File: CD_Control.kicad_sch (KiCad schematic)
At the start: 61 parts, among them Q10 ASR65R046EFD, Q11 ASR65R046EFD, Q12 ASR65R046EFD, Q13 ASR65R046EFD, Q14 ASR65R046EFD, Q15 ASR65R046EFD, Q16 ASR65R046EFD, Q17 AO3400A, Q18 AO3400A, Q19 ASR65R046EFD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

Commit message: More sims, more buildout
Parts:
- added R35: 0.3mR, symbol ct_lib:SEWF3951DL300P9
- added R36: 0Ω, PCM_JLCPCB:R_0402, symbol PCM_JLCPCB-Resistors:0402,0Ω
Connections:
- net GND: now also R36.1
- net PACK_NEGATIVE renamed GNDPWR
- net GNDPWR: now also R35.1
- new net CELLS_NEGATIVE: R35.2, R36.2
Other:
- note added: "Current gain, helps turn-on time Optional"
- note added: "Fast turn-off Optional"
- note added: "Measure range: +/-667 A Trip range: +/-1,667 A"
- note added: "TODO"
- note removed: "Current gain, helps turn-on time"
- note removed: "Fast turn-off"

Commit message: isolated comms
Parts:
- JP1, JP2: footprint Jumper:SolderJumper-2_P1.3mm_Open_TrianglePad1.0x1.5mm -> Jumper:SolderJumper-2_P1.3mm_Open_RoundedPad1.0x1.5mm
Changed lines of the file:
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@@
 			)
 		)
-		(property "Footprint" "Jumper:SolderJumper-2_P1.3mm_Open_TrianglePad1.0x1.5mm"
+		(property "Footprint" "Jumper:SolderJumper-2_P1.3mm_Open_RoundedPad1.0x1.5mm"
 			(at 125.73 213.36 0)
 			(effects
@@
 			)
 		)
-		(property "Footprint" "Jumper:SolderJumper-2_P1.3mm_Open_TrianglePad1.0x1.5mm"
+		(property "Footprint" "Jumper:SolderJumper-2_P1.3mm_Open_RoundedPad1.0x1.5mm"
 			(at 210.82 193.04 0)
 			(effects

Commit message: rolled back TO commit caa5444, didn't mean to roll THAT back
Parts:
- removed D14, D16: D, symbol Device:D
- added D16: MMSZ5246B, PCM_JLCPCB:D_SOD-123, symbol PCM_JLCPCB-Diodes:Zener,MMSZ5246B
- added D22: SMCJ100A_C42371542, JLCImport:SMCJ100A_C42371542, symbol JLCImport:SMCJ100A_C42371542
- added Q22: FQD3P50TM, PCM_JLCPCB:TO-252-2_L6.5-W6.1-P4.58-LS10.0-TL, symbol JLCImport:FQD3P50TM
- added R71, R72, R73: 620R, PCM_JLCPCB:R_1206, symbol ct_lib:1206W4F6200T5E
- added R76: 47kΩ, PCM_JLCPCB:R_0402, symbol PCM_JLCPCB-Resistors:0402,47kΩ
- added R77: 10MΩ, PCM_JLCPCB:R_0402, symbol PCM_JLCPCB-Resistors:0402,10MΩ
- added U10: SMCJ440A_C5294117, PCM_JLCPCB:SOIC-8_L4.9-W3.9-P1.27-LS6.0-BL, symbol JLCImport:SMCJ440A_C5294117
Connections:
- net GNDPWR: now also U10.1 (C)
- net PACK_POSITIVE: now also C11.2, D22.1 (C), R71.2
- net PDSG_GATE_CTRL: now also R76.2
- net at Q10.3 (D), Q11.3 (D), Q12.3 (D)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: now also D16.2, Q22.3 (S), R77.1
- new net: R72.1, R73.1
- new net: R72.2, R73.2
- new net: D22.2 (A), U10.2 (A)
- new net: D16.1, Q22.1 (G), R76.1, R77.2
- new net: Q22.2 (D), R71.1
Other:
- note added: "100V to -440V"
- note added: "500V_SD"
- note added: "650V_DS"
- note added: "Charge"
- note added: "Clamp gate w/ negative terminal voltage"
- note added: "Discharge"
- note added: "Precharge"
- note removed: "120? up 440 down"
- note removed: "450V_DS"
- note removed: "Clamp gate w/ negative terminal voltage Limit: -450V"
- note removed: "Precharge circuit?"
- note removed: "SMBJ440A"
- note removed: "TODO"
- moved on the sheet: C11, C9, D10, D11, D12, D13, D15, D7, D8, D9, JP1, JP2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

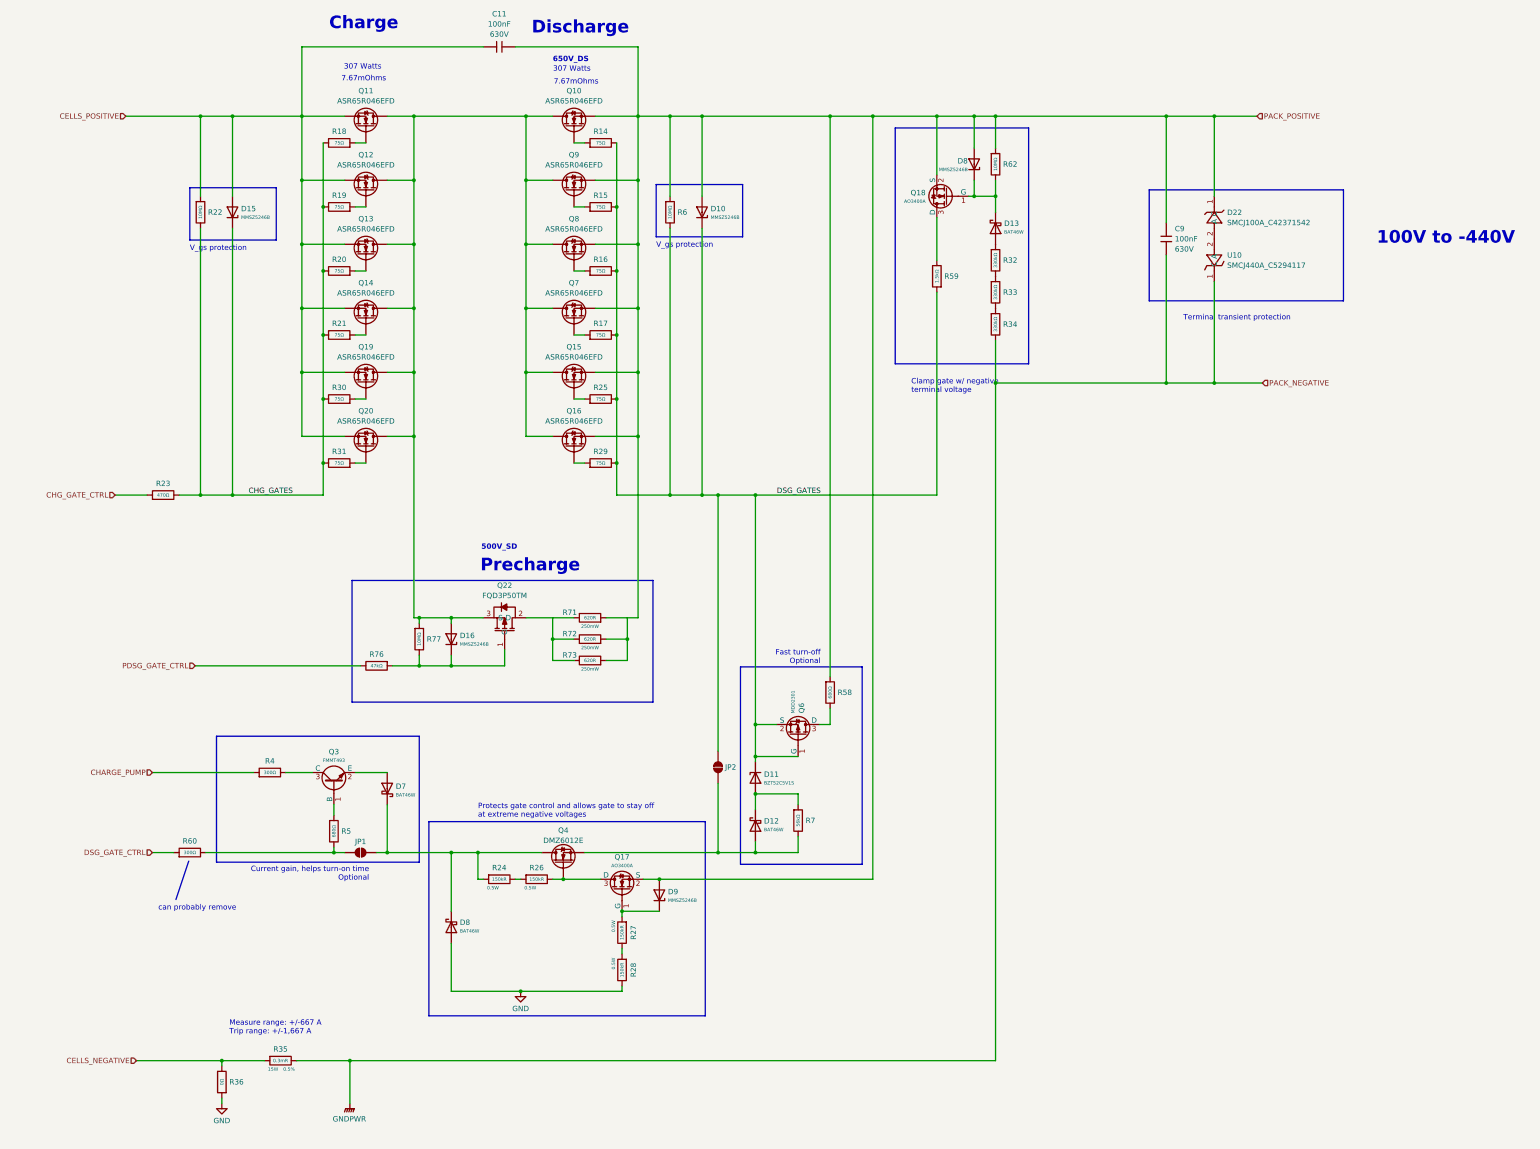
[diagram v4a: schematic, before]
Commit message: prepping for split into 2 boards
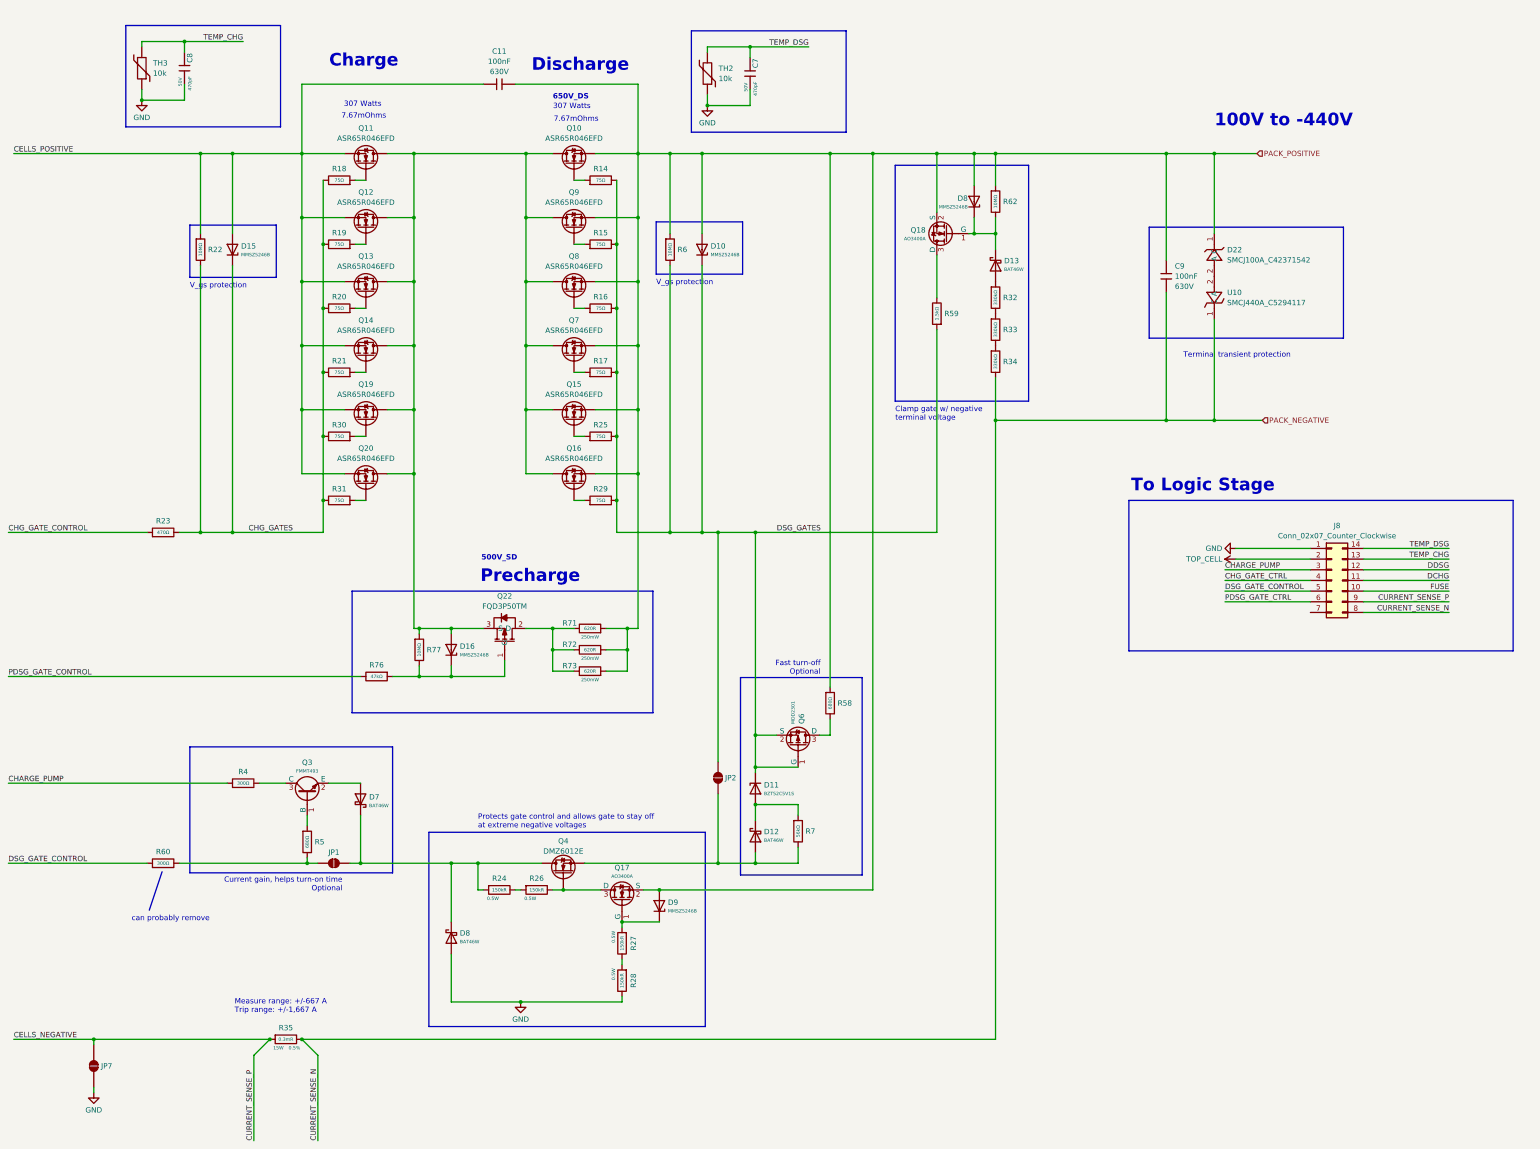
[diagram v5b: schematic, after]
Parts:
- removed R36: 0Ω, PCM_JLCPCB:R_0402, symbol PCM_JLCPCB-Resistors:0402,0Ω
- added C7, C8: 470pF, PCM_JLCPCB:C_0402, symbol PCM_JLCPCB-Capacitors:0402,470pF
- added J8: Conn_02x07_Counter_Clockwise, symbol Connector_Generic:Conn_02x07_Counter_Clockwise
- added JP7: SolderJumper_2_Open, Jumper:SolderJumper-2_P1.3mm_Open_RoundedPad1.0x1.5mm, symbol Jumper:SolderJumper_2_Open
- added TH2, TH3: 10k, PCM_JLCPCB:R_0402, symbol ct_lib:B57232V5103F360
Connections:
- net CELLS_NEGATIVE: now also J8.9 (Pin_9), JP7.2 (B)
- net CHARGE_PUMP: now also J8.3 (Pin_3)
- net CHG_GATE_CTRL: now also J8.4 (Pin_4); no longer R23.1
- net GND: now also C7.2, C8.2, J8.1 (Pin_1), JP7.1 (A), TH2.1, TH3.1
- net PACK_POSITIVE: now also R72.2, R73.2
- net PDSG_GATE_CTRL: now also J8.6 (Pin_6); no longer R76.2
- net at R72.1, R73.1: now also Q22.2 (D), R71.1
- net DSG_GATE_CTRL renamed DSG_GATE_CONTROL
- net DSG_GATE_CONTROL: now also J8.5 (Pin_5)
- net GNDPWR renamed PACK_NEGATIVE
- net PACK_NEGATIVE: now also J8.8 (Pin_8)
- new net CHG_GATE_CONTROL: R23.1
- new net DCHG: J8.11 (Pin_11)
- new net DDSG: J8.12 (Pin_12)
- new net FUSE: J8.10 (Pin_10)
- new net PDSG_GATE_CONTROL: R76.2
- new net TEMP_CHG: C8.1, J8.13 (Pin_13), TH3.2
- new net TEMP_DSG: C7.1, J8.14 (Pin_14), TH2.2
- new net TOP_CELL: J8.2 (Pin_2)
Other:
- note added: "To Logic Stage"
- moved on the sheet: C11, C9, D10, D11, D12, D13, D15, D16, D22, D7, D8, D9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
